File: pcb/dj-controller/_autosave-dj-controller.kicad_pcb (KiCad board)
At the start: 2 copper layers, 1 part, among them U1 CD74HC4067M

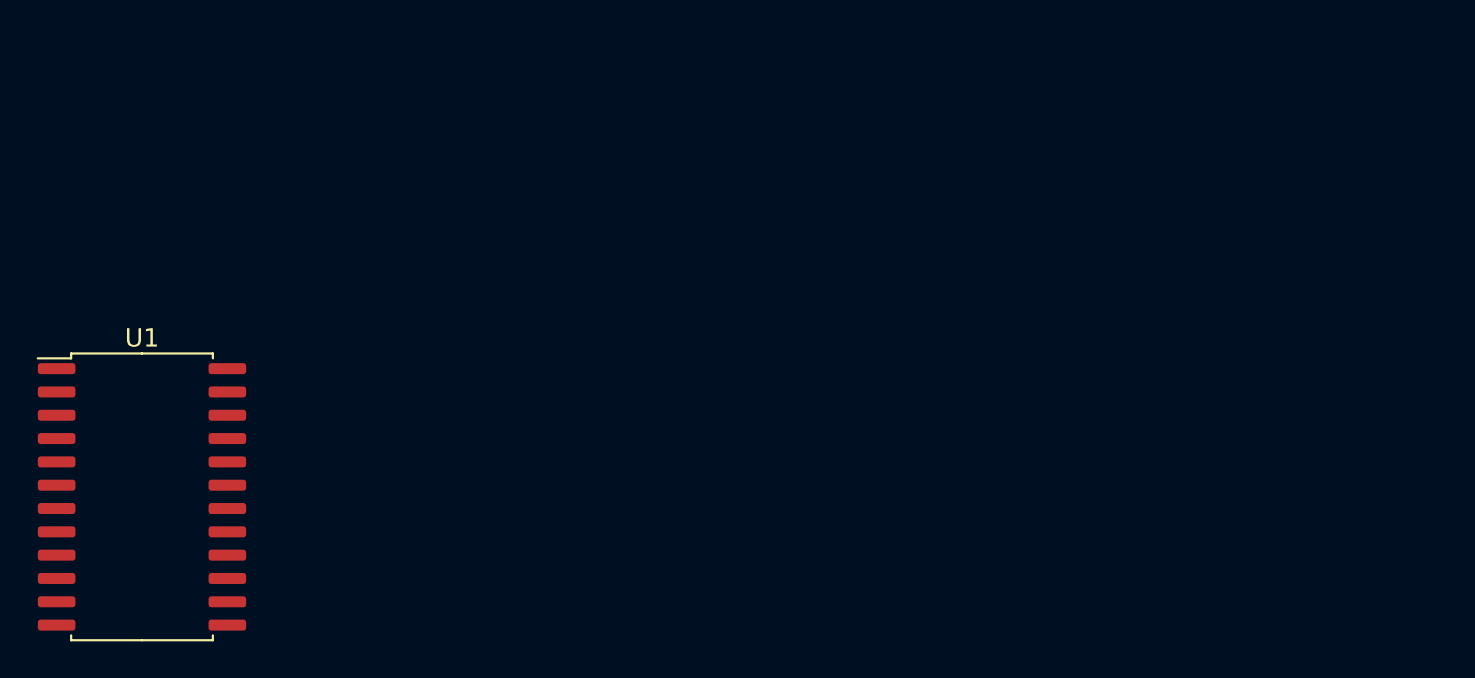
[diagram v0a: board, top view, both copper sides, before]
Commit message: Added 16 potentiometers, cannot get connections right
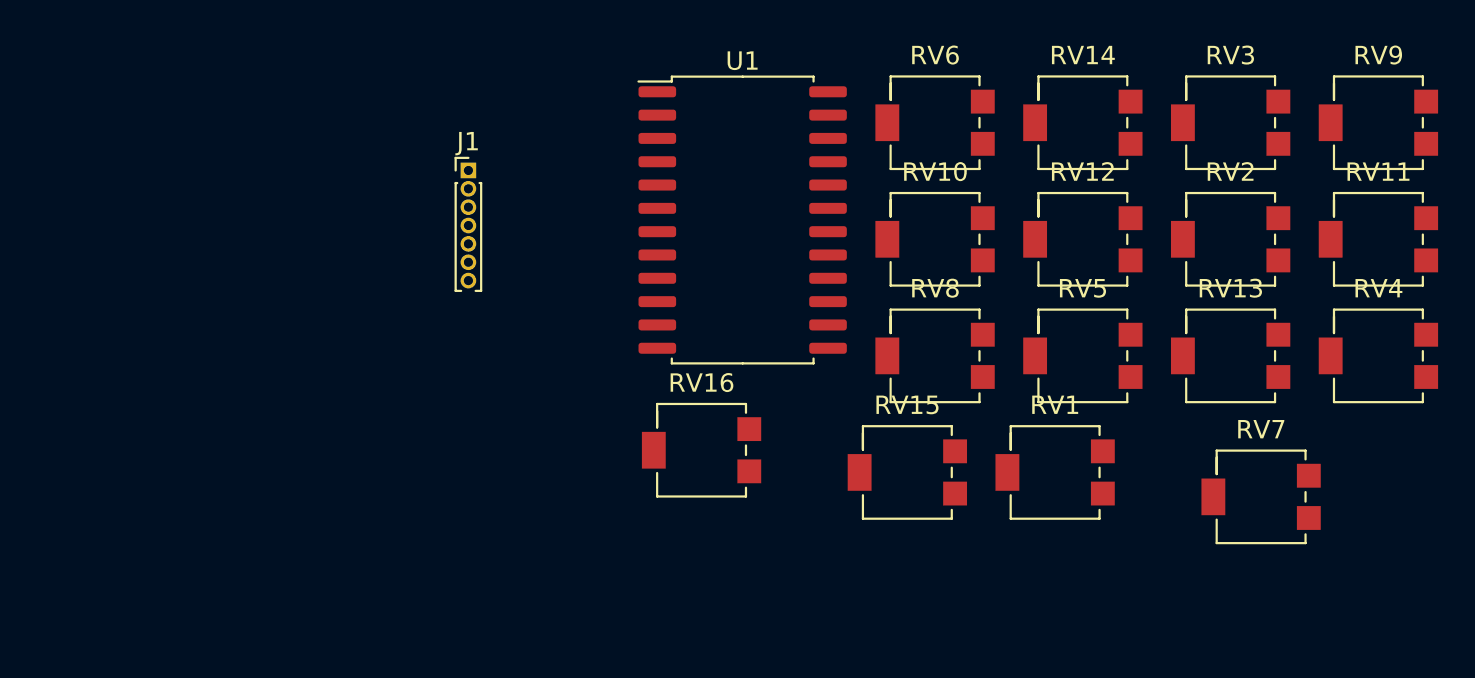
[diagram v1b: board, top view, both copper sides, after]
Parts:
- added J1: Conn_01x07_Male, Connector_PinHeader_1.00mm:PinHeader_1x07_P1.00mm_Vertical, F.Cu at (86.4, 43.2)
- added RV1: R_Potentiometer, Potentiometer_SMD:Potentiometer_Bourns_3214G_Horizontal, F.Cu at (118.3, 59.6)
- added RV10: R_Potentiometer, Potentiometer_SMD:Potentiometer_Bourns_3214G_Horizontal, F.Cu at (111.8, 46.9)
- added RV11: R_Potentiometer, Potentiometer_SMD:Potentiometer_Bourns_3214G_Horizontal, F.Cu at (135.9, 46.9)
- added RV12: R_Potentiometer, Potentiometer_SMD:Potentiometer_Bourns_3214G_Horizontal, F.Cu at (119.8, 46.9)
- added RV13: R_Potentiometer, Potentiometer_SMD:Potentiometer_Bourns_3214G_Horizontal, F.Cu at (127.9, 53.3)
- added RV14: R_Potentiometer, Potentiometer_SMD:Potentiometer_Bourns_3214G_Horizontal, F.Cu at (119.8, 40.6)
- added RV15: R_Potentiometer, Potentiometer_SMD:Potentiometer_Bourns_3214G_Horizontal, F.Cu at (110.3, 59.6)
- added RV16: R_Potentiometer, Potentiometer_SMD:Potentiometer_Bourns_3214G_Horizontal, F.Cu at (99.1, 58.4)
- added RV2: R_Potentiometer, Potentiometer_SMD:Potentiometer_Bourns_3214G_Horizontal, F.Cu at (127.9, 46.9)
- added RV3: R_Potentiometer, Potentiometer_SMD:Potentiometer_Bourns_3214G_Horizontal, F.Cu at (127.9, 40.6)
- added RV4: R_Potentiometer, Potentiometer_SMD:Potentiometer_Bourns_3214G_Horizontal, F.Cu at (135.9, 53.3)
- added RV5: R_Potentiometer, Potentiometer_SMD:Potentiometer_Bourns_3214G_Horizontal, F.Cu at (119.8, 53.3)
- added RV6: R_Potentiometer, Potentiometer_SMD:Potentiometer_Bourns_3214G_Horizontal, F.Cu at (111.8, 40.6)
- added RV7: R_Potentiometer, Potentiometer_SMD:Potentiometer_Bourns_3214G_Horizontal, F.Cu at (129.5, 61.0)
- added RV8: R_Potentiometer, Potentiometer_SMD:Potentiometer_Bourns_3214G_Horizontal, F.Cu at (111.8, 53.3)
- added RV9: R_Potentiometer, Potentiometer_SMD:Potentiometer_Bourns_3214G_Horizontal, F.Cu at (135.9, 40.6)
- moved U1 36.0 mm to (101.3, 45.9)
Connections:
- U1 pad 1: unconnected-(U1-Pad1) -> Net-(U1-Pad1)
- U1 pad 10: unconnected-(U1-Pad10) -> Net-(U1-Pad10)
- U1 pad 11: unconnected-(U1-Pad11) -> Net-(U1-Pad11)
- U1 pad 13: unconnected-(U1-Pad13) -> Net-(U1-Pad13)
- U1 pad 14: unconnected-(U1-Pad14) -> Net-(U1-Pad14)
- U1 pad 16: unconnected-(U1-Pad16) -> Net-(U1-Pad16)
- U1 pad 17: unconnected-(U1-Pad17) -> Net-(U1-Pad17)
- U1 pad 18: unconnected-(U1-Pad18) -> Net-(U1-Pad18)
- U1 pad 19: unconnected-(U1-Pad19) -> Net-(U1-Pad19)
- U1 pad 2: unconnected-(U1-Pad2) -> VCC
- U1 pad 20: unconnected-(U1-Pad20) -> Net-(U1-Pad20)
- U1 pad 21: unconnected-(U1-Pad21) -> Net-(U1-Pad21)
- U1 pad 22: unconnected-(U1-Pad22) -> Net-(U1-Pad22)
- U1 pad 23: unconnected-(U1-Pad23) -> Net-(U1-Pad23)
- U1 pad 24: +3.3V -> VCC
- U1 pad 3: unconnected-(U1-Pad3) -> Net-(U1-Pad3)
- U1 pad 4: unconnected-(U1-Pad4) -> Net-(U1-Pad4)
- U1 pad 5: unconnected-(U1-Pad5) -> Net-(U1-Pad5)
- U1 pad 6: unconnected-(U1-Pad6) -> Net-(U1-Pad6)
- U1 pad 7: Net-(RV1-Pad2) -> Net-(U1-Pad7)
- U1 pad 8: GND -> Net-(U1-Pad8)
- U1 pad 9: Net-(RV1-Pad2) -> Net-(U1-Pad9)
